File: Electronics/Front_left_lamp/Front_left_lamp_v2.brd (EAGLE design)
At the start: 42.9 x 26.7 mm, 9 parts

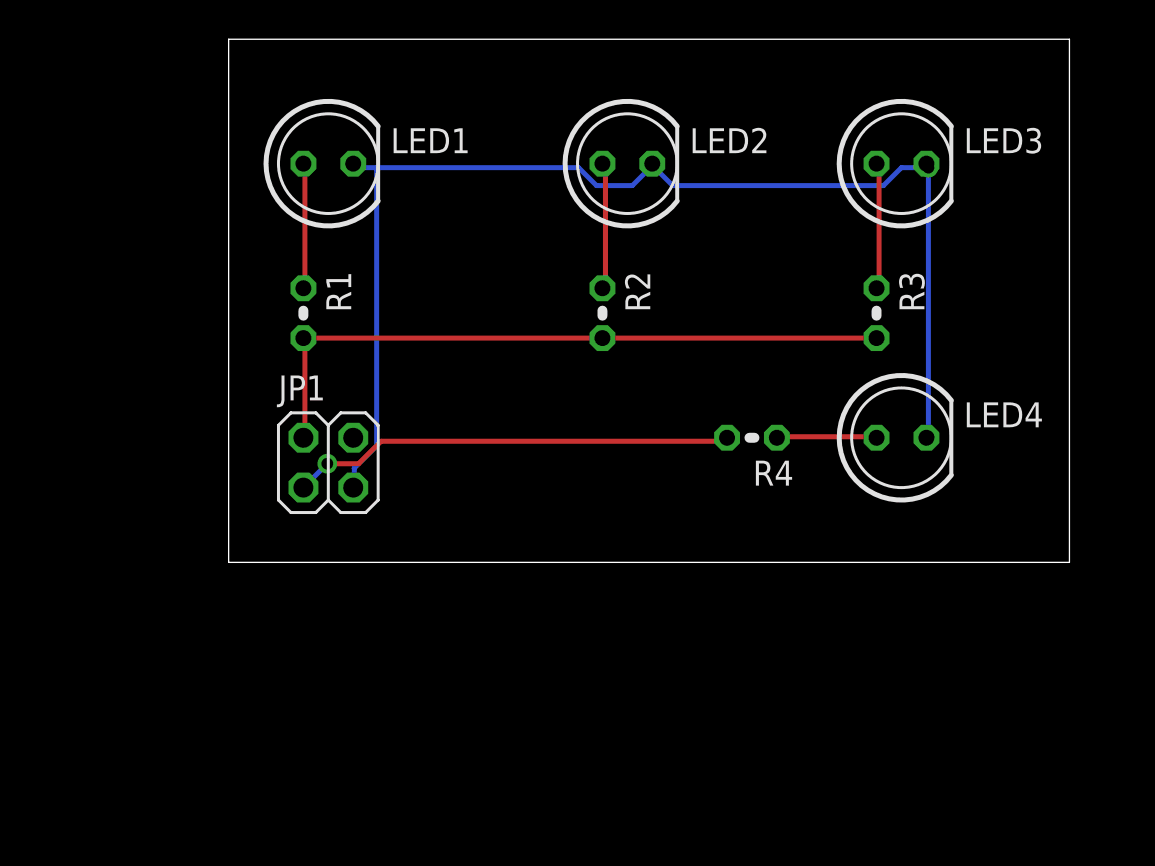
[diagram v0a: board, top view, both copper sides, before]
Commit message: Front lamps done
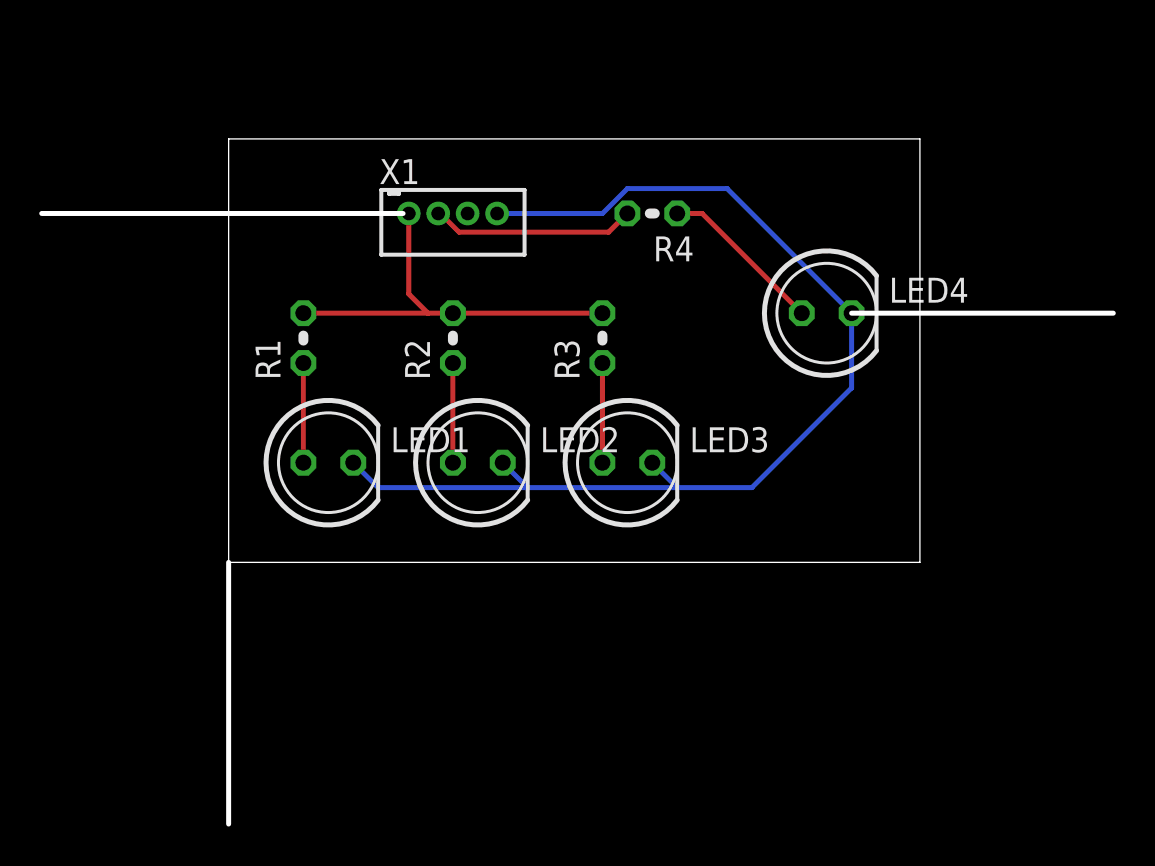
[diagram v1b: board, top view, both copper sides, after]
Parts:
- removed JP1: 2X2, pinhead:2X02
- added X1: B4B-ZR, con-jst:B4B-ZR
- LED1, LED2, LED3: value 2.58V -> 2.58 V
- LED4: value 2.88V -> 1.88 V
- R4: value 1K -> 680
- moved LED3 20.7 mm to (20.3, 5.08)
- moved LED2 17.0 mm to (12.7, 5.08)
- moved LED1 15.2 mm to (5.08, 5.08)
- moved R3 14.0 mm to (19.1, 11.4), turned to 90 degrees
- moved R4 12.5 mm to (21.6, 17.8)
- moved R2 7.73 mm to (11.4, 11.4), turned to 90 degrees
- moved LED4 7.41 mm to (30.5, 12.7)
- moved R1 1.27 mm to (3.81, 11.4), turned to 90 degrees
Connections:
- net N$5: now also X1.1; no longer JP1.2
- net N$6: now also X1.2; no longer JP1.1
- net N$7: now also X1.4; no longer JP1.3
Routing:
- net N$5: track 34.3 -> 20.7 mm
- net N$6: track 22.7 -> 10.4 mm, vias 1 -> 0
- net N$7: track 62.1 -> 56.7 mm, vias 2 -> 0
- net N$4: track 5.10 -> 8.45 mm
- net N$2: track 6.45 -> 5.08 mm
- net N$3: track 6.42 -> 5.08 mm
- net N$1: track 6.38 -> 5.08 mm
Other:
- board size 42.9 x 26.7 mm -> 54.6 x 34.9 mm

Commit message: Front and rear lamps done
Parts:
- X1: value B4B-ZR -> JST-XH-03-PIN-ROUND-PAD; device con-jst:B4B-ZR -> Rembrandt Electronics - JST XH Connectors v1-0:JST-XH-03-PACKAGE-ROUND-PAD
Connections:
- net N$5 renamed API_START_ENGINE
- net N$6 renamed API_TURN_LEFT
- removed net N$7: LED1.K, LED2.K, LED3.K, LED4.K, X1.4
- new net GND: LED1.K, LED2.K, LED3.K, LED4.K, X1.3
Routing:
- net N$7: track 56.7 -> 0.00 mm
- net GND: track 0.00 -> 56.4 mm
- net API_TURN_LEFT: track 10.4 -> 9.68 mm
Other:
- board size 54.6 x 34.9 mm -> 35.2 x 21.6 mm
